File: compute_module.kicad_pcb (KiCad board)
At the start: 2 copper layers, 93.2 x 49 mm, 42 parts, among them J1 2001-1-2-21-00-BK, P1 POWER, P2 HOST, P3 CAM1, Q1 2N7002P.215, Q2 DMP3056L-7, Q3 2N7002P.215, U1 REG1117-3.3, U2 REG1117A-2.5, U3 REG1117A-1.8

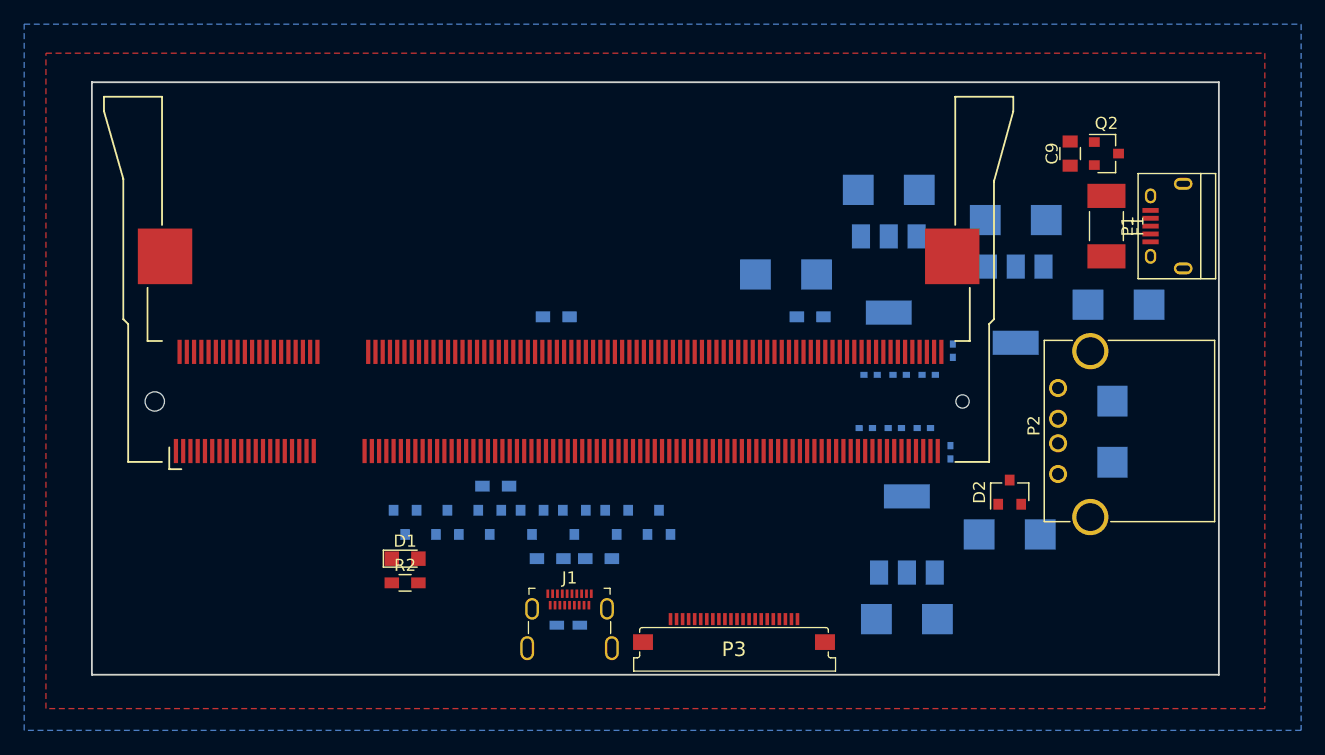
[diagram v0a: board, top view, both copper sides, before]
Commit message: Replaced HDMI connector
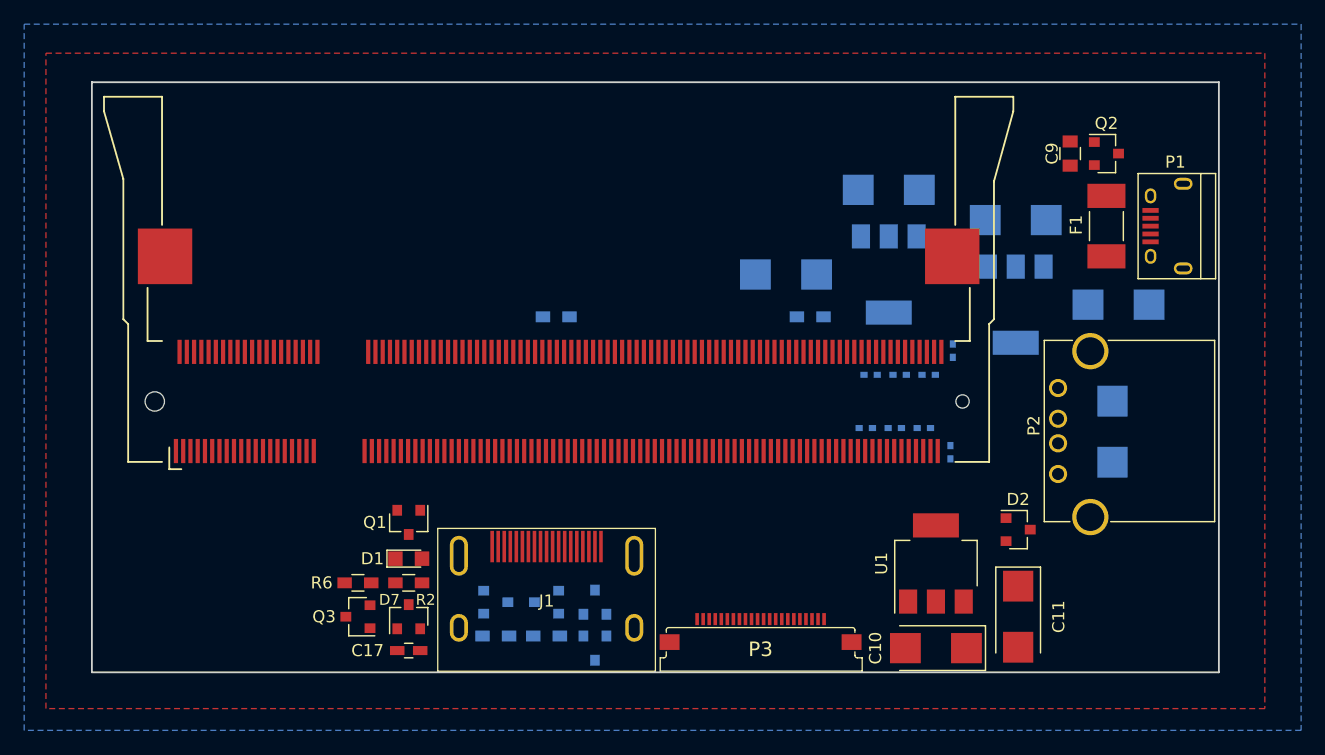
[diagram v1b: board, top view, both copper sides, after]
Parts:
- C10, C11, C17, D7, Q1, Q3, R6, U1: moved to F.Cu
- J1: footprint digikey-footprints:HDMI_Female_DC3RX19JA3R1700 -> HDMI_MOLEX:HDMI_MOLEX_471510001
- moved R6 13.9 mm to (109.6, 99.0), turned to 0 degrees
- moved C17 13.4 mm to (113.8, 104.6), turned to 180 degrees
- moved D6 12.0 mm to (121.0, 100.6), turned to 0 degrees
- moved D3 11.7 mm to (129.2, 104.4), turned to 270 degrees
- moved Q3 10.8 mm to (109.6, 101.8), turned to 180 degrees
- moved R5 10.6 mm to (121.0, 103.4)
- moved D7 10.3 mm to (113.8, 101.8), turned to 90 degrees
- moved C11 6.84 mm to (164.2, 101.8), turned to 270 degrees
- moved D4 6.82 mm to (129.2, 100.6), turned to 90 degrees
- moved D5 6.71 mm to (125.2, 100.6), turned to 180 degrees
- moved R4 6.41 mm to (125.2, 103.4)
- moved J1 4.34 mm to (125.2, 96.0)
- moved C10 3.39 mm to (157.4, 104.4), turned to 180 degrees
- moved U1 3.39 mm to (157.4, 97.4)
- moved D2 3.18 mm to (164.2, 94.6), turned to 0 degrees
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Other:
- board size 93.2 x 49 mm -> 93.2 x 48.8 mm

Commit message: Moved more components to the top
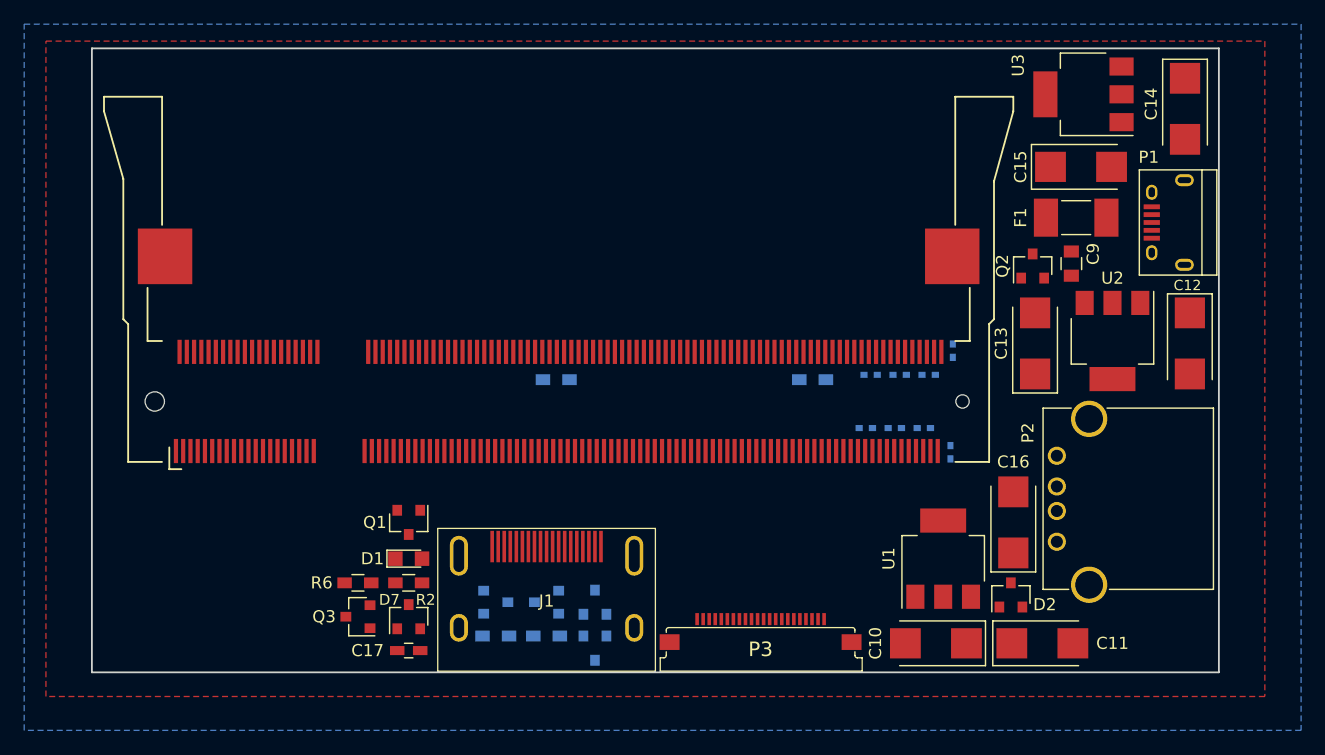
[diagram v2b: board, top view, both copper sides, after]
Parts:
- C12, C13, C14, C15, C16, U2, U3: moved to F.Cu
- moved C15 26.0 mm to (169.4, 64.6), turned to 0 degrees
- moved C14 25.4 mm to (178.0, 59.8), turned to 270 degrees
- moved U3 21.9 mm to (169.6, 58.6), turned to 180 degrees
- moved C12 17.6 mm to (178.4, 79.2), turned to 270 degrees
- moved Q2 11.1 mm to (165.4, 72.8), turned to 90 degrees
- moved C16 11.1 mm to (163.8, 94.0)
- moved C9 9.10 mm to (168.6, 72.6)
- moved U2 8.54 mm to (172.0, 79.0)
- moved C13 7.61 mm to (165.6, 79.2), turned to 90 degrees
- moved P2 5.60 mm to (167.4, 95.6)
- moved D2 5.43 mm to (163.6, 100.0), turned to 90 degrees
- moved R3 5.20 mm to (147.2, 82.2)
- moved R1 5.20 mm to (126.0, 82.2)
- moved C11 2.97 mm to (166.2, 104.0), turned to 0 degrees
- moved F1 2.60 mm to (169.0, 68.8), turned to 0 degrees
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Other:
- board size 93.2 x 48.8 mm -> 93.2 x 51.6 mm

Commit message: Fixed fused
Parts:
- C17: footprint Capacitors_SMD:C_0603_HandSoldering -> Capacitors_SMD:C_0402
- F1: value 2.5A -> 2A 6V; footprint Fuse_Holders_and_Fuses:Fuse_CB61F -> Polyfuse_Bourns_MF-PSML:Polyfuse_0805
- moved C9 4.39 mm to (164.6, 70.8)
- moved F1 3.61 mm to (172.0, 70.8), turned to 270 degrees
- moved Q2 3.52 mm to (168.3, 70.8), turned to 0 degrees
- moved C15 0.57 mm to (169.0, 65.0)
- moved U3 0.57 mm to (169.2, 59.0)
- moved C17 0.40 mm to (113.8, 104.2)
- moved P2 0.30 mm to (167.7, 95.6)
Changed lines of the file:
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@@
   )
   (module Capacitors_SMD:C_0805 (layer F.Cu)
-    (at 168.6 72.6 90)
+    (at 164.6 70.8 90)
     (descr "Capacitor SMD 0805, reflow soldering, AVX (see smccp.pdf)")
     (tags "capacitor 0805")
     (attr smd)
-    (fp_text reference C9 (at 0.8 1.8 90) (layer F.SilkS)
+    (fp_text reference C9 (at 2.6 0 180) (layer F.SilkS)
       (effects (font (size 1 1) (thickness 0.15)))
     )
@@
       (effects (font (size 1 1) (thickness 0.15)))
     )
-    (fp_text user %R (at 0.8 1.8 90) (layer F.Fab)
+    (fp_text user %R (at 2.6 0 180) (layer F.Fab)
       (effects (font (size 1 1) (thickness 0.15)))
     )
@@
     (tags "capacitor tantalum smd")
     (attr smd)
-    (fp_text reference C13 (at 0 -2.8 90) (layer F.SilkS)
+    (fp_text reference C13 (at 5 0 180) (layer F.SilkS)
       (effects (font (size 1 1) (thickness 0.15)))
     )
@@
   )
   (module Capacitors_Tantalum_SMD:CP_Tantalum_Case-C_EIA-6032-28_Reflow (layer F.Cu)
-    (at 169.4 64.6)
+    (at 169 65)
     (descr "Tantalum capacitor, Case C, EIA 6032-28, 6.0x3.2x2.5mm, Reflow soldering footprint")
     (tags "capacitor tantalum smd")
@@
       (net 2 GND))
     (model Capacitors_Tantalum_SMD.3dshapes/CP_Tantalum_Case-C_EIA-6032-28.wrl
-      (at (xyz 0 0 0))
-      (scale (xyz 1 1 1))
-      (rotate (xyz 0 0 0))
-    )
-  )
-  (module Capacitors_SMD:C_0603_HandSoldering (layer F.Cu)
-    (at 113.8 104.6 180)
-    (descr "Capacitor SMD 0603, hand soldering")
-    (tags "capacitor 0603")
-    (attr smd)
-    (fp_text reference C17 (at 3.4 0 180) (layer F.SilkS)
-      (effects (font (size 1 1) (thickness 0.15)))
-    )
-    (fp_text value 100nF (at 0 1.5 180) (layer F.Fab)
-      (effects (font (size 1 1) (thickness 0.15)))
-    )
-    (fp_text user %R (at 3.4 0 180) (layer F.Fab)
-      (effects (font (size 1 1) (thickness 0.15)))
-    )
-    (fp_line (start -0.8 0.4) (end -0.8 -0.4) (layer F.Fab) (width 0.1))
-    (fp_line (start 0.8 0.4) (end -0.8 0.4) (layer F.Fab) (width 0.1))
-    (fp_line (start 0.8 -0.4) (end 0.8 0.4) (layer F.Fab) (width 0.1))
-    (fp_line (start -0.8 -0.4) (end 0.8 -0.4) (layer F.Fab) (width 0.1))
-    (fp_line (start -0.35 -0.6) (end 0.35 -0.6) (layer F.SilkS) (width 0.12))
-    (fp_line (start 0.35 0.6) (end -0.35 0.6) (layer F.SilkS) (width 0.12))
-    (fp_line (start -1.8 -0.65) (end 1.8 -0.65) (layer F.CrtYd) (width 0.05))
-    (fp_line (start -1.8 -0.65) (end -1.8 0.65) (layer F.CrtYd) (width 0.05))
-    (fp_line (start 1.8 0.65) (end 1.8 -0.65) (layer F.CrtYd) (width 0.05))
-    (fp_line (start 1.8 0.65) (end -1.8 0.65) (layer F.CrtYd) (width 0.05))
-    (pad 1 smd rect (at -0.95 0 180) (size 1.2 0.75) (layers F.Cu F.Paste F.Mask)
-      (net 7 "Net-(C17-Pad1)"))
-    (pad 2 smd rect (at 0.95 0 180) (size 1.2 0.75) (layers F.Cu F.Paste F.Mask)
-      (net 2 GND))
-    (model Capacitors_SMD.3dshapes/C_0603.wrl
       (at (xyz 0 0 0))
       (scale (xyz 1 1 1))
@@
     )
   )
-  (module Fuse_Holders_and_Fuses:Fuse_CB61F (layer F.Cu)
-    (at 169 68.8)
-    (descr "CB61F Series")
-    (tags Fuse)
-    (attr smd)
-    (fp_text reference F1 (at -4.6 0 270) (layer F.SilkS)
-      (effects (font (size 1 1) (thickness 0.15)))
-    )
-    (fp_text value 2.5A (at 0 2.6) (layer F.Fab)
-      (effects (font (size 1 1) (thickness 0.15)))
-    )
-    (fp_line (start -3.75 1.85) (end -3.75 -1.85) (layer F.CrtYd) (width 0.05))
-    (fp_line (start 3.75 1.85) (end -3.75 1.85) (layer F.CrtYd) (width 0.05))
-    (fp_line (start 3.75 -1.85) (end 3.75 1.85) (layer F.CrtYd) (width 0.05))
-    (fp_line (start -3.75 -1.85) (end 3.75 -1.85) (layer F.CrtYd) (width 0.05))
-    (fp_line (start -1.2 1.4) (end 1.2 1.4) (layer F.SilkS) (width 0.12))
-    (fp_line (start -1.2 -1.4) (end 1.2 -1.4) (layer F.SilkS) (width 0.12))
-    (fp_line (start -3.05 1.28) (end -3.05 -1.28) (layer F.Fab) (width 0.1))
-    (fp_line (start 3.05 1.28) (end -3.05 1.28) (layer F.Fab) (width 0.1))
-    (fp_line (start 3.05 -1.28) (end 3.05 1.28) (layer F.Fab) (width 0.1))
-    (fp_line (start -3.05 -1.28) (end 3.05 -1.28) (layer F.Fab) (width 0.1))
-    (pad 1 smd rect (at -2.5 0) (size 2 3.15) (layers F.Cu F.Paste F.Mask)
-      (net 16 "Net-(F1-Pad1)"))
-    (pad 2 smd rect (at 2.5 0) (size 2 3.15) (layers F.Cu F.Paste F.Mask)
-      (net 17 "Net-(F1-Pad2)"))
-  )
   (module Connectors:USB_Micro-B (layer F.Cu)
     (at 176.6 69.2 90)
@@
   )
   (module Connectors:USB_A (layer F.Cu)
-    (at 167.4 95.6 90)
+    (at 167.7 95.6 90)
     (descr "USB A connector")
     (tags "USB USB_A")
@@
   )
   (module TO_SOT_Packages_SMD:SOT-23 (layer F.Cu)
-    (at 165.4 72.8 90)
+    (at 168.3 70.8)
     (descr "SOT-23, Standard")
     (tags SOT-23)
     (attr smd)
-    (fp_text reference Q2 (at 0 -2.5 90) (layer F.SilkS)
-      (effects (font (size 1 1) (thickness 0.15)))
-    )
-    (fp_text value DMP3056L-7 (at 0 2.5 90) (layer F.Fab)
-      (effects (font (size 1 1) (thickness 0.15)))
-    )
-    (fp_text user %R (at 0 0 180) (layer F.Fab)
+    (fp_text reference Q2 (at -0.1 -2.6) (layer F.SilkS)
+      (effects (font (size 1 1) (thickness 0.15)))
+    )
+    (fp_text value DMP3056L-7 (at 0 2.5) (layer F.Fab)
+      (effects (font (size 1 1) (thickness 0.15)))
+    )
+    (fp_text user %R (at 0 0 90) (layer F.Fab)
       (effects (font (size 0.5 0.5) (thickness 0.075)))
     )
@@
     (fp_line (start 0.76 -1.58) (end -1.4 -1.58) (layer F.SilkS) (width 0.12))
     (fp_line (start 0.76 1.58) (end -0.7 1.58) (layer F.SilkS) (width 0.12))
-    (pad 1 smd rect (at -1 -0.95 90) (size 0.9 0.8) (layers F.Cu F.Paste F.Mask)
-      (net 2 GND))
-    (pad 2 smd rect (at -1 0.95 90) (size 0.9 0.8) (layers F.Cu F.Paste F.Mask)
+    (pad 1 smd rect (at -1 -0.95) (size 0.9 0.8) (layers F.Cu F.Paste F.Mask)
+      (net 2 GND))
+    (pad 2 smd rect (at -1 0.95) (size 0.9 0.8) (layers F.Cu F.Paste F.Mask)
       (net 5 +5V))
-    (pad 3 smd rect (at 1 0 90) (size 0.9 0.8) (layers F.Cu F.Paste F.Mask)
+    (pad 3 smd rect (at 1 0) (size 0.9 0.8) (layers F.Cu F.Paste F.Mask)
       (net 16 "Net-(F1-Pad1)"))
     (model ${KISYS3DMOD}/TO_SOT_Packages_SMD.3dshapes/SOT-23.wrl
@@
   )
   (module TO_SOT_Packages_SMD:SOT-223-3_TabPin2 (layer F.Cu)
-    (at 169.6 58.6 180)
+    (at 169.2 59 180)
     (descr "module CMS SOT223 4 pins")
     (tags "CMS SOT")
@@
       (net 2 GND))
   )
+  (module Capacitors_SMD:C_0402 (layer F.Cu)
+    (at 113.8 104.2 180)
+    (descr "Capacitor SMD 0402, reflow soldering, AVX (see smccp.pdf)")
+    (tags "capacitor 0402")
+    (attr smd)
+    (fp_text reference C17 (at 0 -1.27 180) (layer F.SilkS)
+      (effects (font (size 1 1) (thickness 0.15)))
+    )
+    (fp_text value 100nF (at 0 1.27 180) (layer F.Fab)
+      (effects (font (size 1 1) (thickness 0.15)))
+    )
+    (fp_text user %R (at 0 -1.27 180) (layer F.Fab)
+      (effects (font (size 1 1) (thickness 0.15)))
+    )
+    (fp_line (start -0.5 0.25) (end -0.5 -0.25) (layer F.Fab) (width 0.1))
+    (fp_line (start 0.5 0.25) (end -0.5 0.25) (layer F.Fab) (width 0.1))
+    (fp_line (start 0.5 -0.25) (end 0.5 0.25) (layer F.Fab) (width 0.1))
+    (fp_line (start -0.5 -0.25) (end 0.5 -0.25) (layer F.Fab) (width 0.1))
+    (fp_line (start 0.25 -0.47) (end -0.25 -0.47) (layer F.SilkS) (width 0.12))
+    (fp_line (start -0.25 0.47) (end 0.25 0.47) (layer F.SilkS) (width 0.12))
+    (fp_line (start -1 -0.4) (end 1 -0.4) (layer F.CrtYd) (width 0.05))
+    (fp_line (start -1 -0.4) (end -1 0.4) (layer F.CrtYd) (width 0.05))
+    (fp_line (start 1 0.4) (end 1 -0.4) (layer F.CrtYd) (width 0.05))
+    (fp_line (start 1 0.4) (end -1 0.4) (layer F.CrtYd) (width 0.05))
+    (pad 1 smd rect (at -0.55 0 180) (size 0.6 0.5) (layers F.Cu F.Paste F.Mask)
+      (net 7 "Net-(C17-Pad1)"))
+    (pad 2 smd rect (at 0.55 0 180) (size 0.6 0.5) (layers F.Cu F.Paste F.Mask)
+      (net 2 GND))
+    (model Capacitors_SMD.3dshapes/C_0402.wrl
+      (at (xyz 0 0 0))
+      (scale (xyz 1 1 1))
+      (rotate (xyz 0 0 0))
+    )
+  )
+  (module Polyfuse_Bourns_MF-PSML:Polyfuse_0805 (layer F.Cu)
+    (at 172 70.8 270)
+    (descr "Fuse, Sicherung, SMD1206, Littlefuse-Wickmann, Reflow,")
+    (tags "Fuse Sicherung SMD1206 Littlefuse-Wickmann Reflow ")
+    (attr smd)
+    (fp_text reference F1 (at -2.6 0 360) (layer F.SilkS)
+      (effects (font (size 1 1) (thickness 0.15)))
+    )
+    (fp_text value "2A 6V" (at -0.45 3.2 270) (layer F.Fab)
+      (effects (font (size 1 1) (thickness 0.15)))
+    )
+    (fp_line (start -1.7 0.85) (end -1.7 -0.85) (layer F.Fab) (width 0.1))
+    (fp_line (start 1.7 0.85) (end -1.7 0.85) (layer F.Fab) (width 0.1))
+    (fp_line (start 1.7 -0.85) (end 1.7 0.85) (layer F.Fab) (width 0.1))
+    (fp_line (start -1.7 -0.85) (end 1.7 -0.85) (layer F.Fab) (width 0.1))
+    (fp_line (start 1 0.87) (end -1 0.87) (layer F.SilkS) (width 0.12))
+    (fp_line (start -1 -0.87) (end 1 -0.87) (layer F.SilkS) (width 0.12))
+    (fp_line (start -1.87 -1) (end 1.87 -1) (layer F.CrtYd) (width 0.05))
+    (fp_line (start -1.87 -1) (end -1.87 1) (layer F.CrtYd) (width 0.05))
+    (fp_line (start 1.87 1) (end 1.87 -1) (layer F.CrtYd) (width 0.05))
+    (fp_line (start 1.87 1) (end -1.87 1) (layer F.CrtYd) (width 0.05))
+    (pad 1 smd rect (at -1.1 0) (size 1.5 1) (layers F.Cu F.Paste F.Mask)
+      (net 16 "Net-(F1-Pad1)"))
+    (pad 2 smd rect (at 1.1 0) (size 1.5 1) (layers F.Cu F.Paste F.Mask)
+      (net 17 "Net-(F1-Pad2)"))
+  )
   (gr_line (start 87.6 106.4) (end 87.6 54.8) (angle 90) (layer Edge.Cuts) (width 0.15))

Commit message: Routed differential pairs for camera and HDMI
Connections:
- net CAM1_CN renamed CAM1_C_N
- net CAM1_CP renamed CAM1_C_P
- net CAM1_DN0 renamed CAM1_D0_N
- net CAM1_DN1 renamed CAM1_D1_N
- net CAM1_DN2 renamed CAM1_D2_N
- net CAM1_DN3 renamed CAM1_D3_N
- net CAM1_DP0 renamed CAM1_D0_P
- net CAM1_DP1 renamed CAM1_D1_P
- net CAM1_DP2 renamed CAM1_D2_P
- net CAM1_DP3 renamed CAM1_D3_P
- net USB_DM renamed USB_D_N
- net USB_DP renamed USB_D_P
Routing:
- net CAM1_D3_N: track 0.00 -> 15.1 mm
- net CAM1_D3_P: track 0.00 -> 15.1 mm
- net CAM1_D2_N: track 0.00 -> 14.9 mm
- net CAM1_D2_P: track 0.00 -> 14.9 mm
- net CAM1_C_N: track 0.00 -> 14.8 mm
- net CAM1_C_P: track 0.00 -> 14.8 mm
- net CAM1_D1_N: track 0.00 -> 14.7 mm
- net CAM1_D1_P: track 0.00 -> 14.7 mm
- net CAM1_D0_N: track 0.00 -> 14.6 mm
- net CAM1_D0_P: track 0.00 -> 14.6 mm
- net HDMI_D2_N: track 0.00 -> 12.9 mm
- net HDMI_D0_N: track 0.00 -> 12.9 mm
- net HDMI_D2_P: track 0.00 -> 12.7 mm
- net HDMI_D0_P: track 0.00 -> 12.7 mm
- net HDMI_D1_N: track 0.00 -> 12.7 mm
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- added copper zone on In1.Cu, net GND
- added copper zone on In2.Cu, net GND
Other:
- copper layers 2 -> 4
- net class Default: clearance 0.2 -> 0.18
- rule trace_clearance: 0.2 -> 0.18
- rule trace_min: 0.16 -> 0.2

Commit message: Routed the rest of the board
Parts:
- moved C11 15.7 mm to (152.0, 97.2), turned to 90 degrees
- moved C7 0.20 mm to (158.8, 88.2)
- moved C1 0.20 mm to (152.0, 82.0)
- moved C2 0.20 mm to (151.6, 86.0)
- moved C3 0.20 mm to (154.4, 82.0)
- moved C4 0.20 mm to (154.0, 86.0)
- moved C5 0.20 mm to (156.8, 82.0)
- moved C6 0.20 mm to (156.4, 86.0)
- moved C8 0.20 mm to (159.0, 79.8)
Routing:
- net +5V: track 0.00 -> 168.0 mm, vias 0 -> 6
- net +3V3: track 0.00 -> 154.4 mm, vias 0 -> 7
- net +1V8: track 0.00 -> 110.5 mm, vias 0 -> 2
- net GND: track 0.00 -> 60.0 mm, vias 0 -> 20
- net CD1_SDA: track 0.00 -> 52.2 mm, vias 0 -> 2
- net CD1_SCL: track 0.00 -> 52.2 mm, vias 0 -> 2
- net CAM1_IO1: track 0.00 -> 51.7 mm, vias 0 -> 2
- net CAM1_IO0: track 0.00 -> 51.7 mm, vias 0 -> 2
- net +2V5: track 0.00 -> 47.8 mm, vias 0 -> 2
- net HDMI_SDA: track 0.00 -> 41.9 mm, vias 0 -> 3
- net HDMI_SCL: track 0.00 -> 41.4 mm, vias 0 -> 4
- net HDMI_HPD_N_1V8: track 0.00 -> 34.1 mm, vias 0 -> 2
- net HDMI_CEC: track 0.00 -> 33.8 mm, vias 0 -> 2
- net Net-(C17-Pad1): track 0.00 -> 26.6 mm, vias 0 -> 2
- net USB_D_P: track 0.00 -> 24.0 mm, vias 0 -> 2
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
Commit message: Stitched ground planes with vias
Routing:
- net GND: track 60.0 -> 360.6 mm, vias 20 -> 57
